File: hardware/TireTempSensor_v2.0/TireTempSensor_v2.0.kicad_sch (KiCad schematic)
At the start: 20 parts, among them J1 SWD_01x06, J2 CAN_01x04, SW1 RESET, U1 STM32L4P5RET6, Y1 16MGHz

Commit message: footprints added
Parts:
- C11: value 0.1u -> 100n; footprint (none) -> Capacitor_SMD:C_0603_1608Metric
- J2: footprint SOLDER_PAD_01x04:SolderWirePad_1x04_SMD_1x2mm -> Connector_PinHeader_1.27mm:PinHeader_1x04_P1.27mm_Vertical
- R11: renamed from 10k1; value 1k -> 10k; footprint (none) -> Resistor_SMD:R_0603_1608Metric
- R3: footprint (none) -> Resistor_SMD:R_0603_1608Metric
- SW1: footprint (none) -> Button:PTS815SJK250SMTRLFS
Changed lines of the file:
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@@
     (property "Reference" "R3" (id 0) (at 248.92 81.28 90))
     (property "Value" "1k" (id 1) (at 248.92 83.82 90))
-    (property "Footprint" "" (id 2) (at 248.92 86.36 0)
+    (property "Footprint" "Resistor_SMD:R_0603_1608Metric" (id 2) (at 248.92 86.36 0)
       (effects (font (size 1.27 1.27)) hide)
     )
@@
     (property "Reference" "SW1" (id 0) (at 240.03 78.74 0))
     (property "Value" "RESET" (id 1) (at 240.03 81.28 0))
-    (property "Footprint" "" (id 2) (at 240.03 81.28 0)
-      (effects (font (size 1.27 1.27)) hide)
-    )
-    (property "Datasheet" "http://www.apem.com/int/index.php?controller=attachment&id_attachment=488" (id 3) (at 240.03 81.28 0)
+    (property "Footprint" "Button:PTS815SJK250SMTRLFS" (id 2) (at 240.03 81.28 0)
+      (effects (font (size 1.27 1.27)) hide)
+    )
+    (property "Datasheet" "https://www.mouser.pl/ProductDetail/CK/PTS815-SJK-250-SMTR-LFS?qs=ahcBuItHZ3yETpGYMHf%2FgQ%3D%3D" (id 3) (at 240.03 81.28 0)
       (effects (font (size 1.27 1.27)) hide)
     )
@@
     (property "Reference" "J2" (id 0) (at 257.81 129.54 0))
     (property "Value" "CAN_01x04" (id 1) (at 257.81 132.08 0))
-    (property "Footprint" "SOLDER_PAD_01x04:SolderWirePad_1x04_SMD_1x2mm" (id 2) (at 257.81 138.43 0)
+    (property "Footprint" "Connector_PinHeader_1.27mm:PinHeader_1x04_P1.27mm_Vertical" (id 2) (at 257.81 138.43 0)
       (effects (font (size 1.27 1.27)) hide)
     )
@@
   (symbol (lib_id "Device:R_Small_US") (at 257.81 83.82 180) (unit 1)
     (in_bom yes) (on_board yes)
-    (property "Reference" "10k1" (id 0) (at 261.62 83.82 0))
-    (property "Value" "1k" (id 1) (at 255.27 83.82 0))
-    (property "Footprint" "" (id 2) (at 257.81 83.82 0)
+    (property "Reference" "R11" (id 0) (at 261.62 81.28 0))
+    (property "Value" "10k" (id 1) (at 261.62 83.82 0))
+    (property "Footprint" "Resistor_SMD:R_0603_1608Metric" (id 2) (at 257.81 83.82 0)
       (effects (font (size 1.27 1.27)) hide)
     )
@@
       (effects (font (size 1.27 1.27)) (justify left))
     )
-    (property "Value" "0.1u" (id 1) (at 251.46 88.9 0)
-      (effects (font (size 1.27 1.27)) (justify left))
-    )
-    (property "Footprint" "" (id 2) (at 257.81 88.9 0)
+    (property "Value" "100n" (id 1) (at 260.35 91.44 0)
+      (effects (font (size 1.27 1.27)) (justify left))
+    )
+    (property "Footprint" "Capacitor_SMD:C_0603_1608Metric" (id 2) (at 257.81 88.9 0)
       (effects (font (size 1.27 1.27)) hide)
     )
@@
   (symbol (lib_id "Device:C_Small") (at 36.83 41.91 0) (unit 1)
     (in_bom yes) (on_board yes)
-    (property "Reference" "C1" (id 0) (at 38.1 40.64 0)
-      (effects (font (size 1.27 1.27)) (justify left))
-    )
-    (property "Value" "4u7" (id 1) (at 38.1 43.18 0)
+    (property "Reference" "C1" (id 0) (at 31.75 40.64 0)
+      (effects (font (size 1.27 1.27)) (justify left))
+    )
+    (property "Value" "4u7" (id 1) (at 31.75 44.45 0)
       (effects (font (size 1.27 1.27)) (justify left))
     )
@@
       (reference "#PWR0137") (unit 1) (value "GND") (footprint "")
     )
-    (path "/8cb6bb84-2302-409b-8462-0657583f850c"
-      (reference "10k1") (unit 1) (value "1k") (footprint "")
-    )
     (path "/f9f9a0d5-067e-4463-98ca-0324d01aab58"
       (reference "C1") (unit 1) (value "4u7") (footprint "Capacitor_SMD:C_0603_1608Metric")
@@
     )
     (path "/cedd5994-edc5-44cf-964a-ec41afe3f067"
-      (reference "C11") (unit 1) (value "0.1u") (footprint "")
+      (reference "C11") (unit 1) (value "100n") (footprint "Capacitor_SMD:C_0603_1608Metric")
     )
     (path "/0f13de77-3258-490a-9a0b-6a199964636d/41874868-33ec-41c1-8167-2f3664e1fe68"
@@
     )
     (path "/0f13de77-3258-490a-9a0b-6a199964636d/864c7f76-4ef9-4c7c-86b8-f769534f69ba"
-      (reference "C16") (unit 1) (value "10u") (footprint "Capacitor_SMD:C_0603_1608Metric")
+      (reference "C16") (unit 1) (value "10u") (footprint "Capacitor_SMD:C_1206_3216Metric")
     )
     (path "/a856e3a9-7561-4cae-8c02-98a27e530f80/e85b7dbf-f4bd-4b03-bf73-4c96c9b60acf"
@@
     )
     (path "/0f13de77-3258-490a-9a0b-6a199964636d/b5ff1b23-f084-4eb0-b287-82c936410df1"
-      (reference "F1") (unit 1) (value "200mA") (footprint "Fuse:Fuse_0805_2012Metric")
+      (reference "F1") (unit 1) (value "200mA") (footprint "Capacitor_SMD:C_1206_3216Metric")
     )
     (path "/68e5b9e0-16b3-4d0c-b881-10c205ad68d8"
@@
       (reference "H4") (unit 1) (value "Mounting_Pad") (footprint "MountingHole:MountingHole_2.7mm_M2.5_ISO14580_Pad")
     )
-    (path "/0f13de77-3258-490a-9a0b-6a199964636d/f5b5f6aa-b44e-4089-b4b2-e5f08e69b5de"
-      (reference "IC1") (unit 1) (value "MAX15462AATA+") (footprint "SON50P300X200X80-8N")
+    (path "/0f13de77-3258-490a-9a0b-6a199964636d/89aaaff4-0310-4bc3-ac15-9a4e83548aea"
+      (reference "IC1") (unit 1) (value "MAX15462AATA+") (footprint "BuckSyncLib:SON50P300X200X80-8N")
     )
     (path "/a856e3a9-7561-4cae-8c02-98a27e530f80/fe7825cf-d398-4618-be5c-f75f78ca9001"
-      (reference "IC2") (unit 1) (value "MLX90621ESF-BAB-000-SP") (footprint "MLX90621ESFBAB000SP")
+      (reference "IC2") (unit 1) (value "MLX90621ESF-BAB-000-SP") (footprint "IRSensor:MLX90621ESFBAB000SP")
     )
     (path "/e83d0d64-0340-470f-821a-01f93e303d55"
@@
     )
     (path "/66a8a3f0-be1e-4f69-ac6b-26c977e68e76"
-      (reference "J2") (unit 1) (value "CAN_01x04") (footprint "SOLDER_PAD_01x04:SolderWirePad_1x04_SMD_1x2mm")
+      (reference "J2") (unit 1) (value "CAN_01x04") (footprint "Connector_PinHeader_1.27mm:PinHeader_1x04_P1.27mm_Vertical")
     )
     (path "/0f13de77-3258-490a-9a0b-6a199964636d/b91ec45a-7128-4fcc-82b0-0a8a3431d89a"
-      (reference "L1") (unit 1) (value "33μH") (footprint "")
+      (reference "L1") (unit 1) (value "33μH") (footprint "Inductor_SMD:L_Vishay_IFSC-1515AH_4x4x1.8mm")
     )
     (path "/0f13de77-3258-490a-9a0b-6a199964636d/73f519ae-782d-4b70-998d-5ecf2082c7c6"
-      (reference "Q1") (unit 1) (value "FQT3P20TF") (footprint "")
+      (reference "Q1") (unit 1) (value "FQT3P20TF") (footprint "Mosfet:SOT-223-4-NFET")
     )
     (path "/277a32e1-817e-421c-85bc-9e97534d3aa8"
@@
     )
     (path "/0d363746-d7d1-4f22-9e2d-6dd88519c16a"
-      (reference "R3") (unit 1) (value "1k") (footprint "")
+      (reference "R3") (unit 1) (value "1k") (footprint "Resistor_SMD:R_0603_1608Metric")
     )
     (path "/f9126d12-525a-4c2b-82ad-a240338a41b0/dc5a9541-e7dd-40b0-a994-7777e8df0600"
-      (reference "R4") (unit 1) (value "1k5") (footprint "")
+      (reference "R4") (unit 1) (value "1k5") (footprint "Resistor_SMD:R_0603_1608Metric")
     )
     (path "/a856e3a9-7561-4cae-8c02-98a27e530f80/3c6d3d4c-7559-40e2-9d79-acc09cf0102f"
@@
     )
     (path "/f9126d12-525a-4c2b-82ad-a240338a41b0/17e28c58-a9d5-45a7-a65e-a7ed3f9fbf3a"
-      (reference "R7") (unit 1) (value "1k5") (footprint "")
+      (reference "R7") (unit 1) (value "1k5") (footprint "Resistor_SMD:R_0603_1608Metric")
     )
     (path "/f9126d12-525a-4c2b-82ad-a240338a41b0/d1d07f77-881a-4220-a312-670fc3f108e7"
-      (reference "R8") (unit 1) (value "1k5") (footprint "")
+      (reference "R8") (unit 1) (value "1k5") (footprint "Resistor_SMD:R_0603_1608Metric")
     )
     (path "/f9126d12-525a-4c2b-82ad-a240338a41b0/b53e7586-4270-4e3a-bf4f-17100a36f7e8"
-      (reference "R9") (unit 1) (value "1k5") (footprint "")
+      (reference "R9") (unit 1) (value "1k5") (footprint "Resistor_SMD:R_0603_1608Metric")
     )
     (path "/f9126d12-525a-4c2b-82ad-a240338a41b0/df5055af-e22c-457b-9688-10f05036ad48"
-      (reference "R10") (unit 1) (value "1k5") (footprint "")
+      (reference "R10") (unit 1) (value "1k5") (footprint "Resistor_SMD:R_0603_1608Metric")
+    )
+    (path "/8cb6bb84-2302-409b-8462-0657583f850c"
+      (reference "R11") (unit 1) (value "10k") (footprint "Resistor_SMD:R_0603_1608Metric")
     )
     (path "/4ab84ec9-d89d-4b72-87da-90888ac6a964"
-      (reference "SW1") (unit 1) (value "RESET") (footprint "")
+      (reference "SW1") (unit 1) (value "RESET") (footprint "Button:PTS815SJK250SMTRLFS")
     )
     (path "/f53b3428-bd08-44fa-84c3-55869b03d735"

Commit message: some pcb connections
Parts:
- J2: footprint Connector_PinHeader_1.27mm:PinHeader_1x04_P1.27mm_Vertical -> Connector_Wire:SolderWire-0.1sqmm_1x04_P3.6mm_D0.4mm_OD1mm_Relief
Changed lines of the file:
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@@
     (property "Reference" "J2" (id 0) (at 257.81 129.54 0))
     (property "Value" "CAN_01x04" (id 1) (at 257.81 132.08 0))
-    (property "Footprint" "Connector_PinHeader_1.27mm:PinHeader_1x04_P1.27mm_Vertical" (id 2) (at 257.81 138.43 0)
+    (property "Footprint" "Connector_Wire:SolderWire-0.1sqmm_1x04_P3.6mm_D0.4mm_OD1mm_Relief" (id 2) (at 257.81 138.43 0)
       (effects (font (size 1.27 1.27)) hide)
     )
@@
     )
     (path "/0f13de77-3258-490a-9a0b-6a199964636d/b5ff1b23-f084-4eb0-b287-82c936410df1"
-      (reference "F1") (unit 1) (value "200mA") (footprint "Capacitor_SMD:C_1206_3216Metric")
+      (reference "F1") (unit 1) (value "200mA") (footprint "Fuse:Fuse_1210_3225Metric")
     )
     (path "/68e5b9e0-16b3-4d0c-b881-10c205ad68d8"
@@
     )
     (path "/66a8a3f0-be1e-4f69-ac6b-26c977e68e76"
-      (reference "J2") (unit 1) (value "CAN_01x04") (footprint "Connector_PinHeader_1.27mm:PinHeader_1x04_P1.27mm_Vertical")
+      (reference "J2") (unit 1) (value "CAN_01x04") (footprint "Connector_Wire:SolderWire-0.1sqmm_1x04_P3.6mm_D0.4mm_OD1mm_Relief")
+    )
+    (path "/0f13de77-3258-490a-9a0b-6a199964636d/9796ff86-39a9-4091-997b-96745af5398a"
+      (reference "JP1") (unit 1) (value "SolderJumper_2_Open") (footprint "Jumper:SolderJumper-2_P1.3mm_Open_TrianglePad1.0x1.5mm")
     )
     (path "/0f13de77-3258-490a-9a0b-6a199964636d/b91ec45a-7128-4fcc-82b0-0a8a3431d89a"

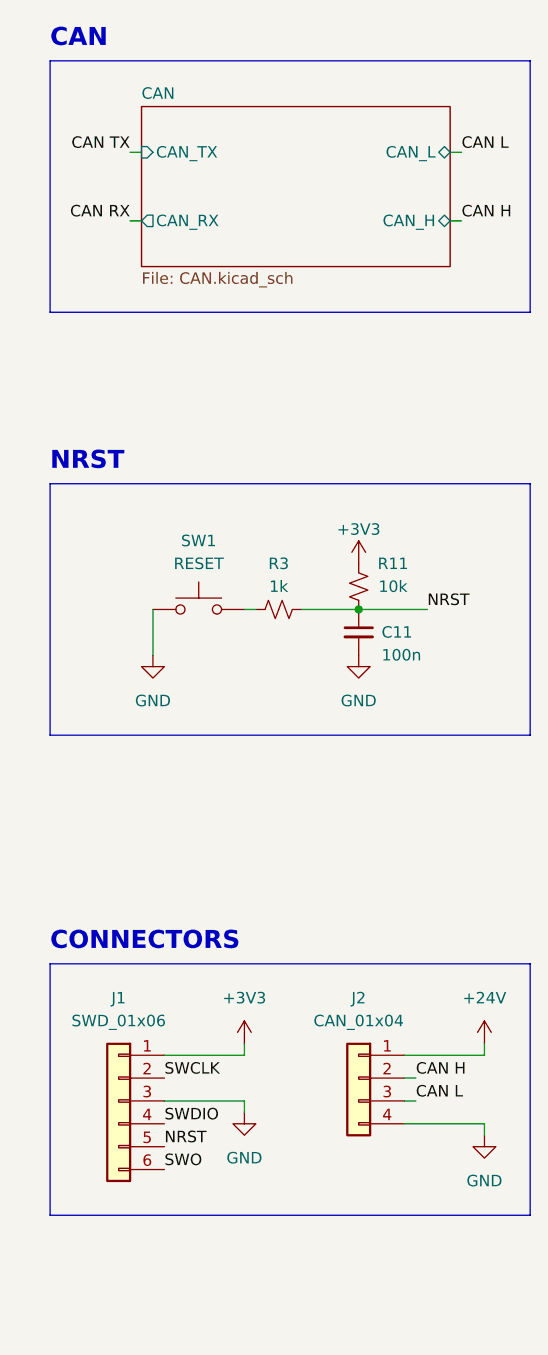
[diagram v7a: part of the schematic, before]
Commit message: more pcb connections
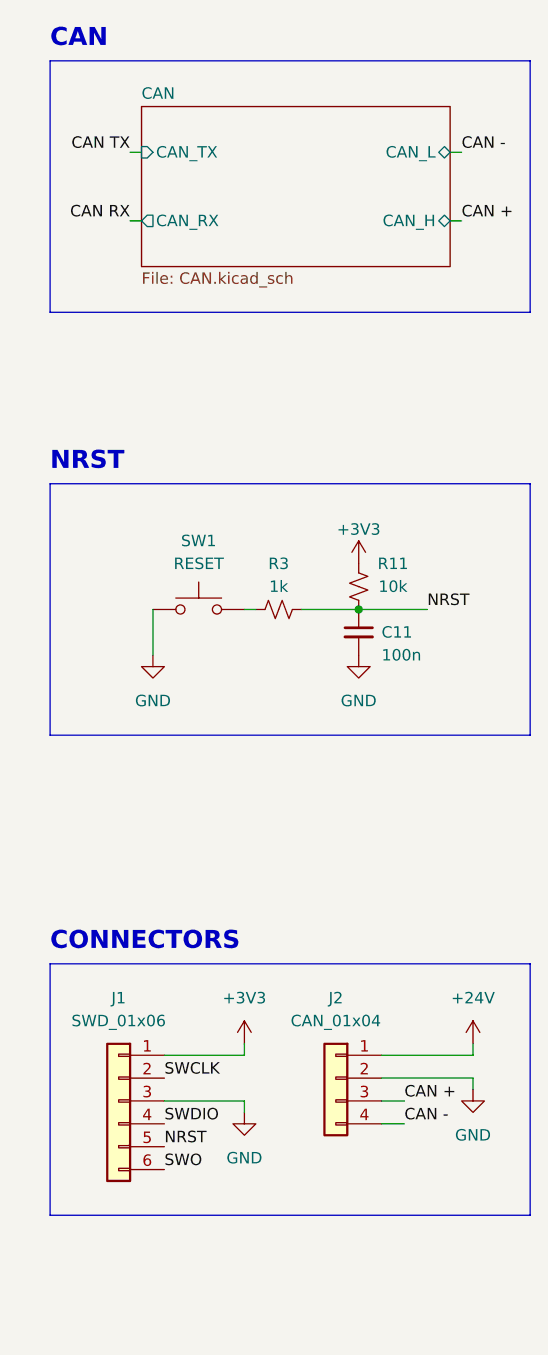
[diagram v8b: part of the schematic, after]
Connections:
- net CAN H is gone; now on net GND: J2.2 (Pin_2)
- net GND: no longer J2.4 (Pin_4)
- net CAN L renamed CAN +
- new net CAN -: J2.4 (Pin_4)
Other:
- moved on the sheet: J2
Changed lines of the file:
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@@
-    (stroke (width 0) (type default) (color 0 0 0 0))
-  )
-  (wire (pts (xy 271.78 143.51) (xy 271.78 144.78))
     (stroke (width 0) (type default) (color 0 0 0 0))
   )
@@
     (stroke (width 0) (type default) (color 0 0 0 0))
   )
-  (wire (pts (xy 262.89 140.97) (xy 264.16 140.97))
+  (wire (pts (xy 260.35 140.97) (xy 262.89 140.97))
     (stroke (width 0) (type default) (color 0 0 0 0))
   )
@@
     (stroke (width 0) (type default) (color 0 0 0 0))
   )
+  (wire (pts (xy 260.35 138.43) (xy 270.51 138.43))
+    (stroke (width 0) (type default) (color 0 0 0 0))
+  )
+  (wire (pts (xy 270.51 138.43) (xy 270.51 139.7))
+    (stroke (width 0) (type default) (color 0 0 0 0))
+  )
   (wire (pts (xy 36.83 44.45) (xy 44.45 44.45))
     (stroke (width 0) (type default) (color 0 0 0 0))
@@
     (stroke (width 0) (type default) (color 0 0 0 0))
   )
-  (wire (pts (xy 271.78 135.89) (xy 271.78 134.62))
+  (wire (pts (xy 270.51 135.89) (xy 270.51 134.62))
     (stroke (width 0) (type default) (color 0 0 0 0))
   )
@@
     (stroke (width 0) (type default) (color 0 0 0 0))
   )
-  (wire (pts (xy 262.89 135.89) (xy 271.78 135.89))
+  (wire (pts (xy 260.35 135.89) (xy 270.51 135.89))
     (stroke (width 0) (type default) (color 0 0 0 0))
   )
@@
     (stroke (width 0) (type default) (color 0 0 0 0))
   )
-  (wire (pts (xy 264.16 138.43) (xy 262.89 138.43))
-    (stroke (width 0) (type default) (color 0 0 0 0))
-  )
   (wire (pts (xy 175.26 36.83) (xy 177.8 36.83))
     (stroke (width 0) (type default) (color 0 0 0 0))
@@
     (stroke (width 0) (type default) (color 0 0 0 0))
   )
+  (wire (pts (xy 260.35 143.51) (xy 262.89 143.51))
+    (stroke (width 0) (type default) (color 0 0 0 0))
+  )
   (wire (pts (xy 36.83 44.45) (xy 36.83 45.72))
     (stroke (width 0) (type default) (color 0 0 0 0))
@@
   )
   (wire (pts (xy 175.26 33.02) (xy 177.8 33.02))
-    (stroke (width 0) (type default) (color 0 0 0 0))
-  )
-  (wire (pts (xy 262.89 143.51) (xy 271.78 143.51))
     (stroke (width 0) (type default) (color 0 0 0 0))
   )
@@
     (effects (font (size 1.27 1.27)) (justify left bottom))
   )
-  (label "CAN L" (at 264.16 140.97 0)
-    (effects (font (size 1.27 1.27)) (justify left bottom))
-  )
   (label "OSC IN" (at 196.85 129.54 0)
     (effects (font (size 1.27 1.27)) (justify left bottom))
@@
     (effects (font (size 1.27 1.27)) (justify left bottom))
   )
-  (label "CAN H" (at 269.24 43.18 0)
+  (label "CAN +" (at 269.24 43.18 0)
     (effects (font (size 1.27 1.27)) (justify left bottom))
   )
@@
     (effects (font (size 1.27 1.27)) (justify left bottom))
   )
-  (label "CAN L" (at 269.24 35.56 0)
+  (label "CAN -" (at 269.24 35.56 0)
     (effects (font (size 1.27 1.27)) (justify left bottom))
   )
@@
   )
   (label "NRST" (at 236.22 146.05 0)
+    (effects (font (size 1.27 1.27)) (justify left bottom))
+  )
+  (label "CAN +" (at 262.89 140.97 0)
     (effects (font (size 1.27 1.27)) (justify left bottom))
   )
@@
     (effects (font (size 1.27 1.27)) (justify right bottom))
   )
-  (label "CAN H" (at 264.16 138.43 0)
-    (effects (font (size 1.27 1.27)) (justify left bottom))
-  )
   (label "NRST" (at 72.39 105.41 180)
     (effects (font (size 1.27 1.27)) (justify right bottom))
@@
   (label "CAN TX" (at 232.41 35.56 180)
     (effects (font (size 1.27 1.27)) (justify right bottom))
+  )
+  (label "CAN -" (at 262.89 143.51 0)
+    (effects (font (size 1.27 1.27)) (justify left bottom))
   )
   (label "CAN TX" (at 110.49 121.92 0)
@@
     (pin "2")
   )
-  (symbol (lib_id "power:GND") (at 271.78 144.78 0) (mirror y) (unit 1)
+  (symbol (lib_id "power:GND") (at 270.51 139.7 0) (mirror y) (unit 1)
     (in_bom yes) (on_board yes) (fields_autoplaced)
-    (property "Reference" "#PWR0105" (id 0) (at 271.78 151.13 0)
-      (effects (font (size 1.27 1.27)) hide)
-    )
-    (property "Value" "GND" (id 1) (at 271.78 149.86 0))
-    (property "Footprint" "" (id 2) (at 271.78 144.78 0)
-      (effects (font (size 1.27 1.27)) hide)
-    )
-    (property "Datasheet" "" (id 3) (at 271.78 144.78 0)
+    (property "Reference" "#PWR?" (id 0) (at 270.51 146.05 0)
+      (effects (font (size 1.27 1.27)) hide)
+    )
+    (property "Value" "GND" (id 1) (at 270.51 144.78 0))
+    (property "Footprint" "" (id 2) (at 270.51 139.7 0)
+      (effects (font (size 1.27 1.27)) hide)
+    )
+    (property "Datasheet" "" (id 3) (at 270.51 139.7 0)
       (effects (font (size 1.27 1.27)) hide)
     )
@@
     (pin "2")
   )
-  (symbol (lib_id "Connector_Generic:Conn_01x04") (at 257.81 138.43 0) (mirror y) (unit 1)
-    (in_bom yes) (on_board yes)
-    (property "Reference" "J2" (id 0) (at 257.81 129.54 0))
-    (property "Value" "CAN_01x04" (id 1) (at 257.81 132.08 0))
-    (property "Footprint" "Connector_Wire:SolderWire-0.1sqmm_1x04_P3.6mm_D0.4mm_OD1mm_Relief" (id 2) (at 257.81 138.43 0)
-      (effects (font (size 1.27 1.27)) hide)
-    )
-    (property "Datasheet" "~" (id 3) (at 257.81 138.43 0)
+  (symbol (lib_id "Connector_Generic:Conn_01x04") (at 255.27 138.43 0) (mirror y) (unit 1)
+    (in_bom yes) (on_board yes)
+    (property "Reference" "J2" (id 0) (at 255.27 129.54 0))
+    (property "Value" "CAN_01x04" (id 1) (at 255.27 132.08 0))
+    (property "Footprint" "Connector_Wire:SolderWire-0.1sqmm_1x04_P3.6mm_D0.4mm_OD1mm_Relief" (id 2) (at 255.27 138.43 0)
+      (effects (font (size 1.27 1.27)) hide)
+    )
+    (property "Datasheet" "~" (id 3) (at 255.27 138.43 0)
       (effects (font (size 1.27 1.27)) hide)
     )
@@
     (pin "1")
   )
-  (symbol (lib_id "power:+24V") (at 271.78 134.62 0) (unit 1)
-    (in_bom yes) (on_board yes)
-    (property "Reference" "#PWR0107" (id 0) (at 271.78 138.43 0)
-      (effects (font (size 1.27 1.27)) hide)
-    )
-    (property "Value" "+24V" (id 1) (at 271.78 129.54 0))
-    (property "Footprint" "" (id 2) (at 271.78 134.62 0)
-      (effects (font (size 1.27 1.27)) hide)
-    )
-    (property "Datasheet" "" (id 3) (at 271.78 134.62 0)
+  (symbol (lib_id "power:+24V") (at 270.51 134.62 0) (unit 1)
+    (in_bom yes) (on_board yes)
+    (property "Reference" "#PWR0107" (id 0) (at 270.51 138.43 0)
+      (effects (font (size 1.27 1.27)) hide)
+    )
+    (property "Value" "+24V" (id 1) (at 270.51 129.54 0))
+    (property "Footprint" "" (id 2) (at 270.51 134.62 0)
+      (effects (font (size 1.27 1.27)) hide)
+    )
+    (property "Datasheet" "" (id 3) (at 270.51 134.62 0)
       (effects (font (size 1.27 1.27)) hide)
     )
@@
       (reference "#PWR0102") (unit 1) (value "GND") (footprint "")
     )
-    (path "/43f7f53f-0c3a-45d4-a3f7-ce43241f5b7c"
-      (reference "#PWR0105") (unit 1) (value "GND") (footprint "")
-    )
     (path "/6b6e55b0-88bf-4ffc-a58b-45186da4d6df"
       (reference "#PWR0106") (unit 1) (value "GND") (footprint "")
@@
       (reference "#PWR0137") (unit 1) (value "GND") (footprint "")
     )
+    (path "/44dc68c2-74b1-466a-8494-831ff7b29f16"
+      (reference "#PWR?") (unit 1) (value "GND") (footprint "")
+    )
     (path "/f9f9a0d5-067e-4463-98ca-0324d01aab58"
